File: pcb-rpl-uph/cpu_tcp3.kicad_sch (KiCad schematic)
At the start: 1 part, among them U5 RPL_UPH_FCBGA1744

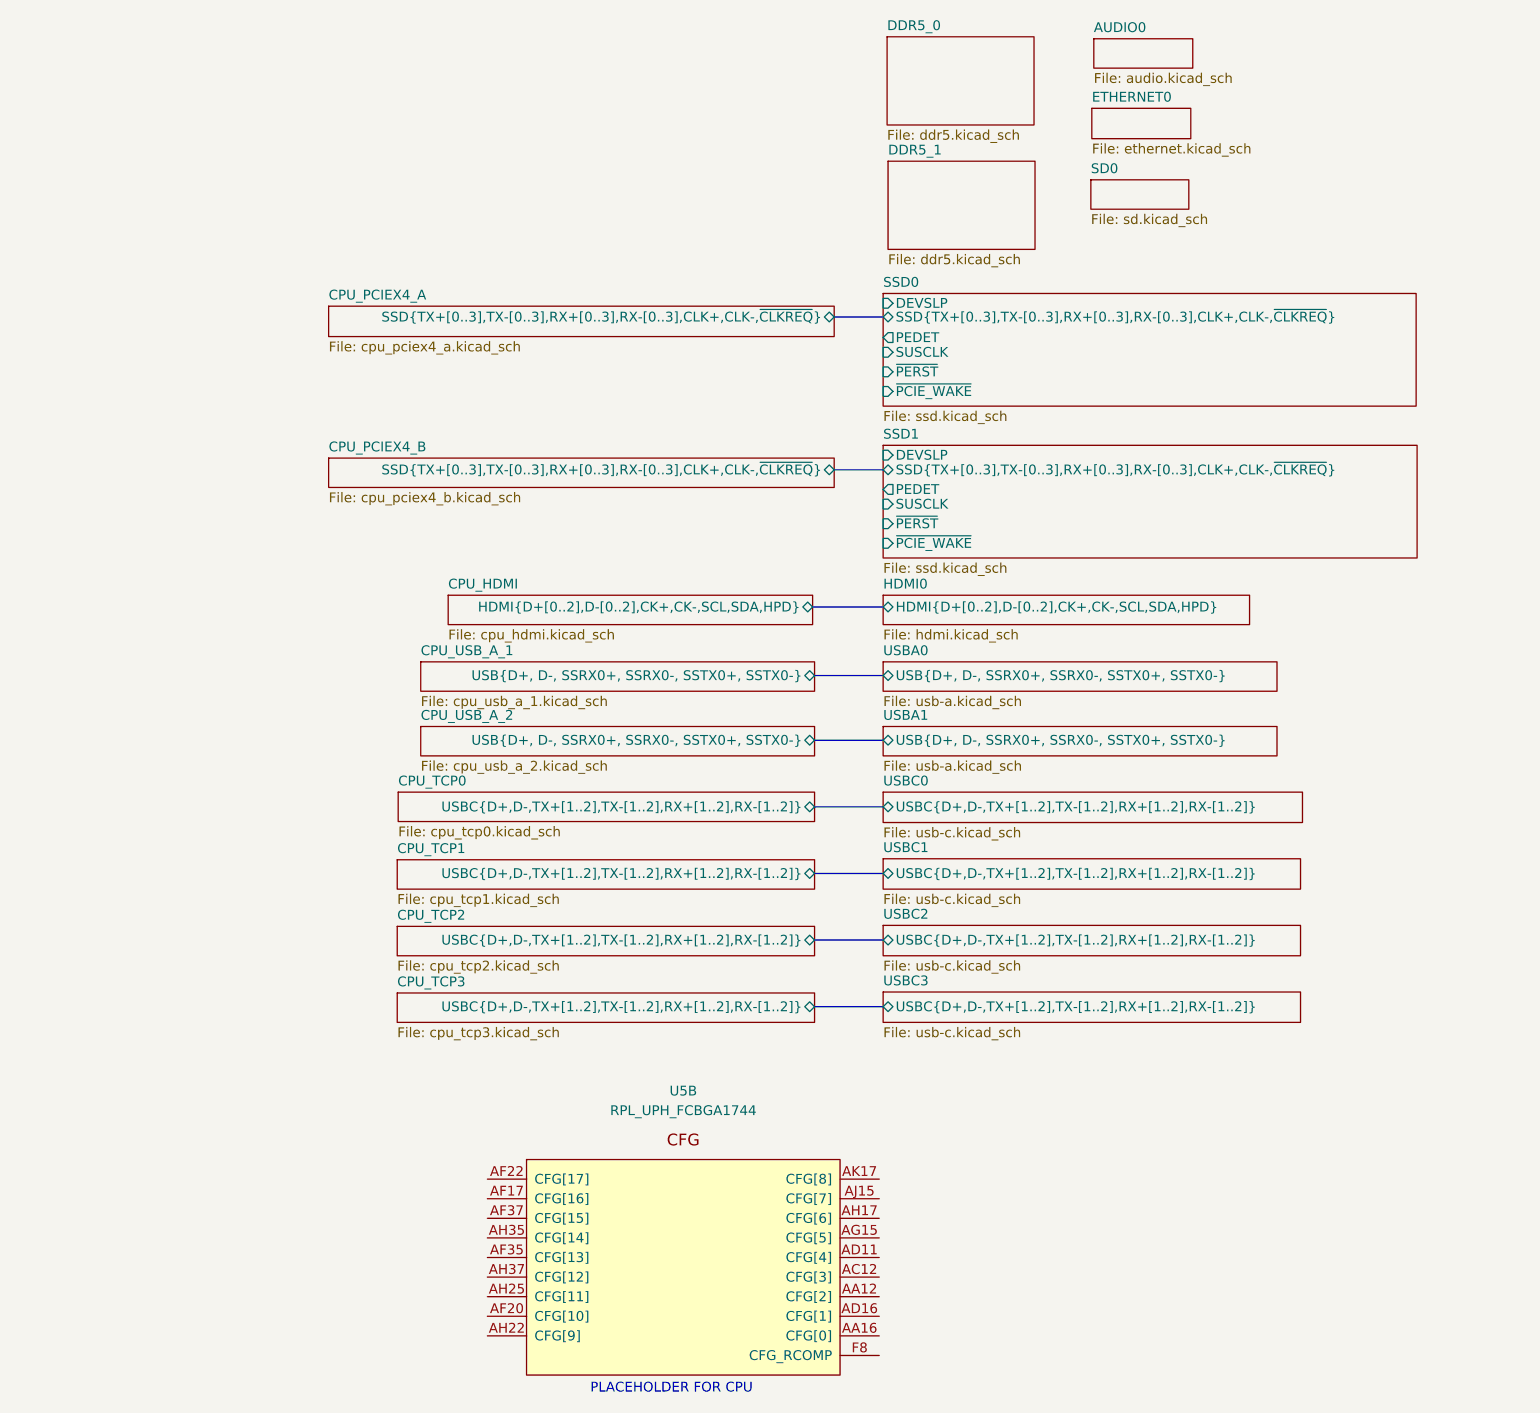
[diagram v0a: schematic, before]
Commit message: Connect USB-A and USB-C data
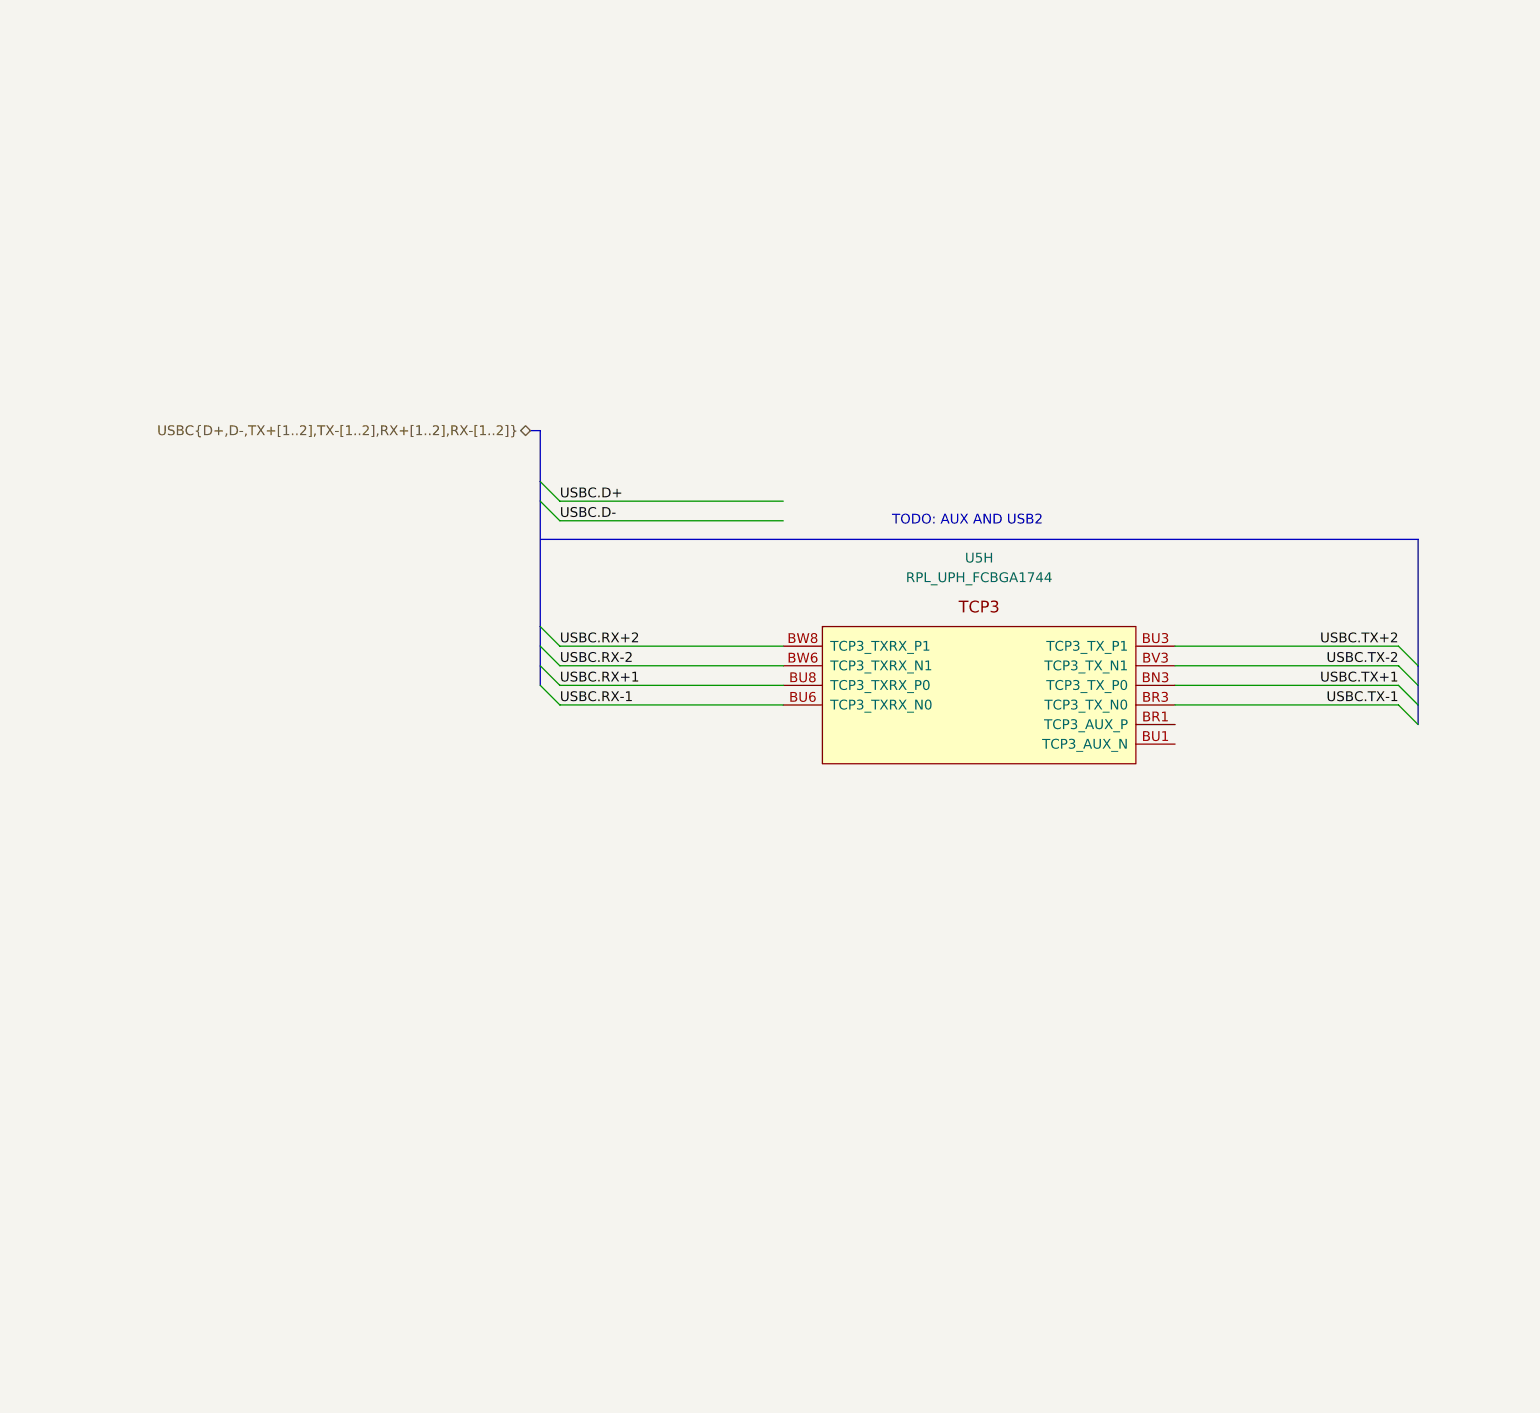
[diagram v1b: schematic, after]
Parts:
- removed U5: RPL_UPH_FCBGA1744, local:RPL_UPH_FCBGA1744, symbol local:RPL_UPH_FCBGA1744
- added U5: RPL_UPH_FCBGA1744, symbol local:RPL_UPH_FCBGA1744
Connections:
- new net USBC.RX+1: U5.BU8 (TCP3_TXRX_P0)
- new net USBC.RX+2: U5.BW8 (TCP3_TXRX_P1)
- new net USBC.RX-1: U5.BU6 (TCP3_TXRX_N0)
- new net USBC.RX-2: U5.BW6 (TCP3_TXRX_N1)
- new net USBC.TX+1: U5.BN3 (TCP3_TX_P0)
- new net USBC.TX+2: U5.BU3 (TCP3_TX_P1)
- new net USBC.TX-1: U5.BR3 (TCP3_TX_N0)
- new net USBC.TX-2: U5.BV3 (TCP3_TX_N1)
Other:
- removed sheet AUDIO0
- removed sheet CPU_HDMI
- removed sheet CPU_PCIEX4_A
- removed sheet CPU_PCIEX4_B
- removed sheet CPU_TCP0
- removed sheet CPU_TCP1
- removed sheet CPU_TCP2
- removed sheet CPU_TCP3
- removed sheet CPU_USB_A_1
- removed sheet CPU_USB_A_2
- removed sheet DDR5_0
- removed sheet DDR5_1
- removed sheet ETHERNET0
- removed sheet HDMI0
- removed sheet SD0
- removed sheet SSD0
- removed sheet SSD1
- removed sheet USBA0
- removed sheet USBA1
- removed sheet USBC0
- removed sheet USBC1
- removed sheet USBC2
- removed sheet USBC3
- note added: "TODO: AUX AND USB2"
- note removed: "PLACEHOLDER FOR CPU"

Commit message: add display connector
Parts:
- U5: footprint (none) -> local:RPL_UPH_FCBGA1744
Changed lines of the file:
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@@
       (effects (font (size 1.27 1.27)))
     )
-    (property "Footprint" "" (at 154.686 88.9 0)
+    (property "Footprint" "local:RPL_UPH_FCBGA1744" (at 154.686 88.9 0)
       (effects (font (size 1.27 1.27)) hide)
     )
